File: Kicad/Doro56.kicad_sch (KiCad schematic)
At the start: 76 parts, among them J1 MJ-4PP-9, SW1 SW_Push_45deg, SW10 SW_Push_45deg, SW11 SW_Push_45deg, SW12 SW_Push_45deg, SW13 SW_Push_45deg, SW14 SW_Push_45deg, SW15 SW_Push_45deg, SW16 SW_Push_45deg, SW17 SW_Push_45deg, SW18 SW_Push_45deg, SW19 SW_Push_45deg, SW2 SW_Push_45deg, SW20 SW_Push_45deg, SW21 SW_Push_45deg, SW22 SW_Push_45deg, SW23 SW_Push_45deg, SW24 SW_Push_45deg, SW25 SW_Push_45deg, SW26 SW_Push_45deg, SW27 SW_Push_45deg, SW28 SW_Push_45deg, SW29 SW_Push_45deg, SW3 SW_Push_45deg, SW30 SW_Push_45deg, SW31 SW_Push_45deg, SW32 SW_Push_45deg, SW33 RotaryEncoder_Switch, SW34 SW_SPDT, SW4 SW_Push_45deg, SW5 SW_Push_45deg, SW6 SW_Push_45deg, SW7 SW_Push_45deg, SW8 SW_Push_45deg, SW9 SW_Push_45deg, U1 ProMicro

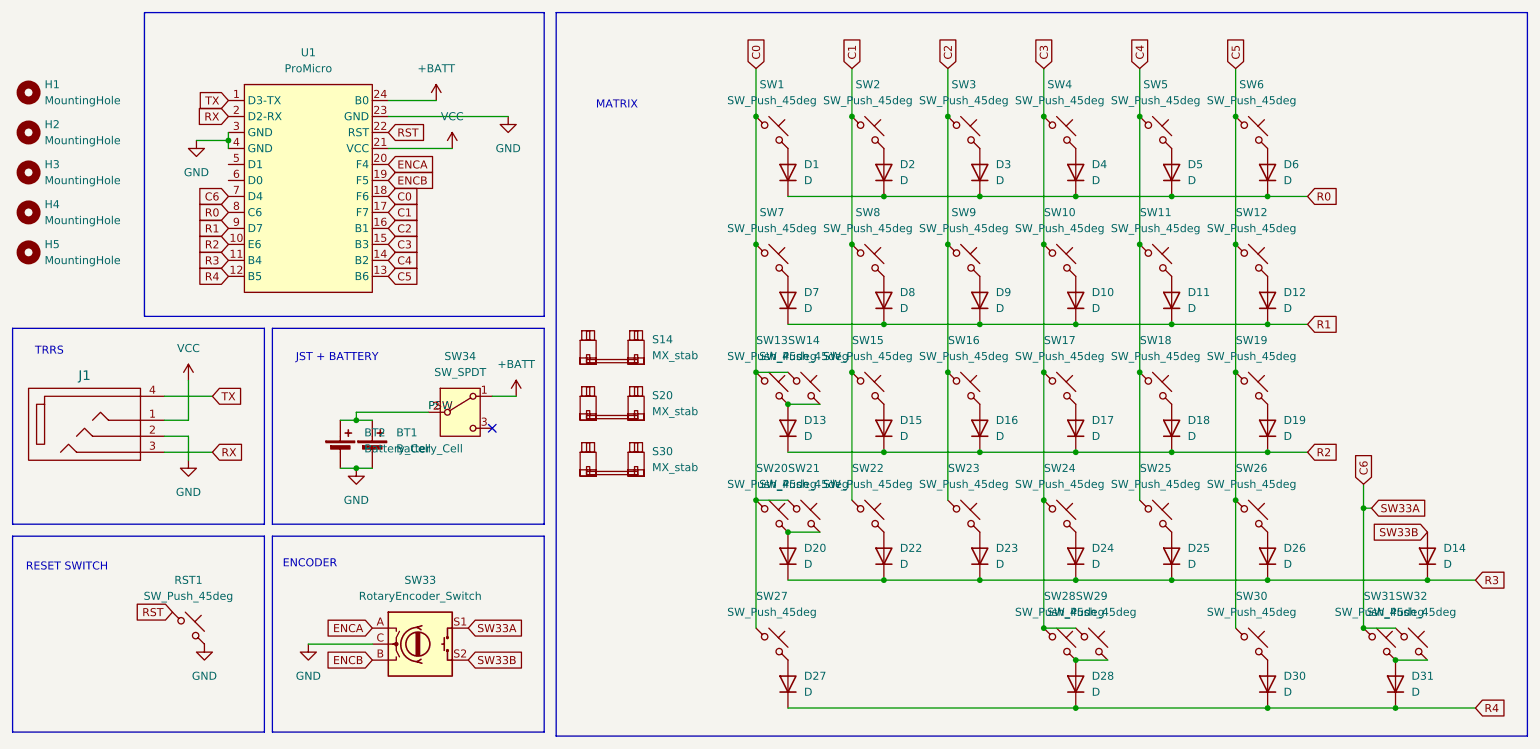
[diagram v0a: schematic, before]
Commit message: v1.1
v1.1 - Minor Edit
Caps and Enter Footprints: Changed to a reversible footprint (previously used two single key footprints rotated).
JST PH Footprint: Adjusted and relocated for increased flexibility.
PCB Cutout: Modified to remove blank space between Control and Alt keys, allowing space for a 402030 battery without increasing the case height clearance.
Plate: Slightly increased the cutout size for the rotary encoder.
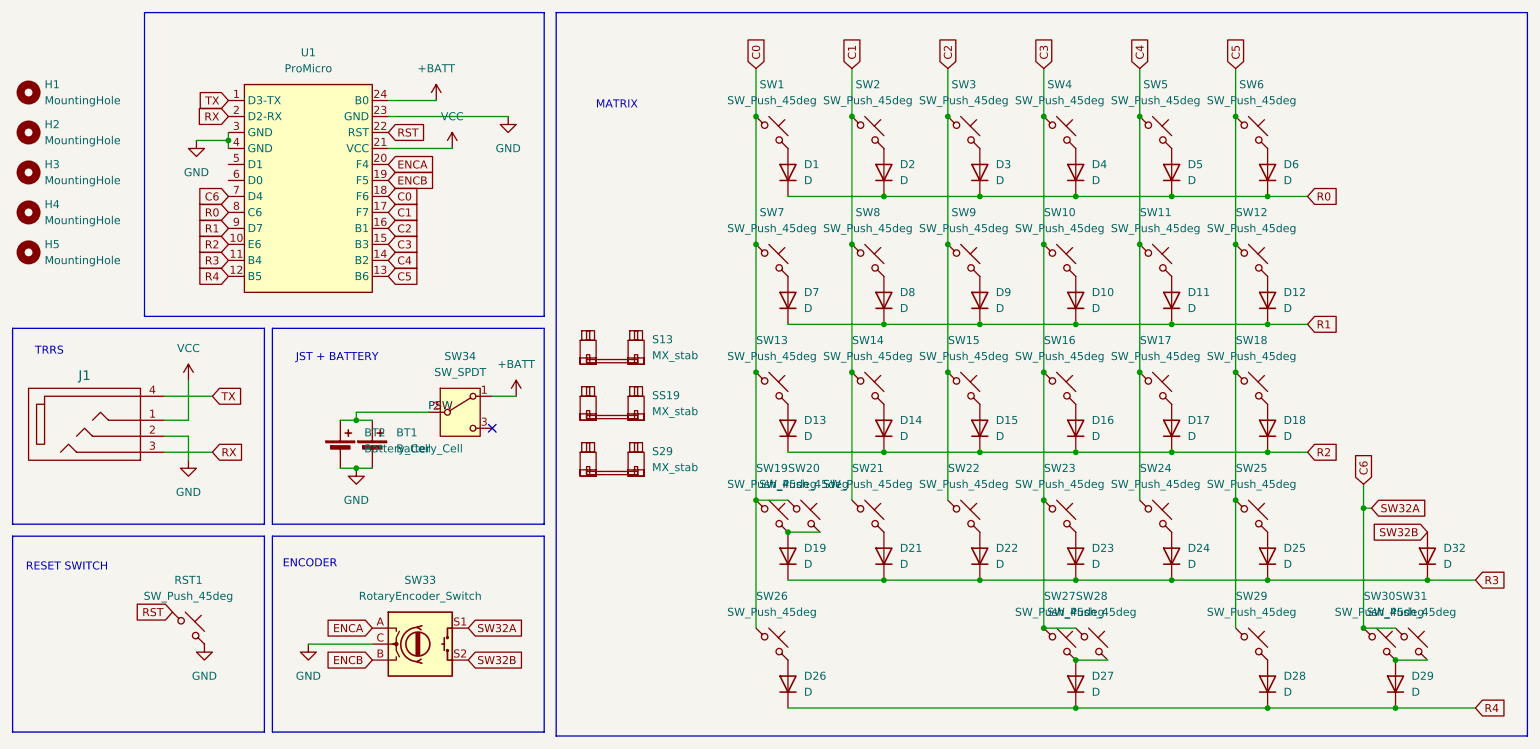
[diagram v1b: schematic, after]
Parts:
- removed SW14: SW_Push_45deg, GHN:MX 2.25U, symbol Switch:SW_Push_45deg
- BT1: footprint GHN:JST_PH_reversible -> GHN:JST_PH_reversible_vert
- SW13: footprint GHN:MX 1.75 STP 1.25 -> GHN:MX Rev 1U
- renumbered D15 to D14, D16 to D15, D17 to D16, D18 to D17, D19 to D18, D20 to D19, D22 to D21, D23 to D22, D24 to D23, D25 to D24, D26 to D25, D27 to D26, D28 to D27, D30 to D28, D31 to D29, D14 to D32, S14 to S13, S30 to S29, S20 to SS19, SW15 to SW14, SW16 to SW15, SW17 to SW16, SW18 to SW17, SW19 to SW18, SW20 to SW19, SW21 to SW20, SW22 to SW21, SW23 to SW22, SW24 to SW23, SW25 to SW24, SW26 to SW25, SW27 to SW26, SW28 to SW27, SW29 to SW28, SW30 to SW29, SW31 to SW30, SW32 to SW31
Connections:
- net SW33B renamed SW32B

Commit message: yeet lego case
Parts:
- renumbered SS19 to S19
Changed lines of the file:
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@@
 		(dnp no)
 		(fields_autoplaced yes)
-		(property "Reference" "SS19"
+		(property "Reference" "S19"
 			(at 142.24 77.3429 0)
 			(effects
@@
 			(project "Doro56"
 				(path "/66443d69-f594-44f0-97f8-81b5f08a0d21"
-					(reference "SS19")
+					(reference "S19")
 					(unit 1)
 				)

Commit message: 1.2
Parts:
- BT1: footprint GHN:JST_PH_reversible_vert -> GHN:JST_PH_2P_Reversible
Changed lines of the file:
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@@
 		(dnp no)
 		(property "Reference" "BT2"
-			(at 96.52 83.2484 0)
+			(at 88.9 83.312 0)
 			(effects
 				(font
@@
 		)
 		(property "Value" "Battery_Cell"
-			(at 96.52 85.7884 0)
+			(at 82.296 87.122 0)
 			(effects
 				(font
@@
 		(dnp no)
 		(property "Reference" "BT1"
-			(at 101.6 83.2484 0)
+			(at 99.822 83.312 0)
 			(effects
 				(font
@@
 		)
 		(property "Value" "Battery_Cell"
-			(at 101.6 85.7884 0)
+			(at 96.52 87.122 0)
 			(effects
 				(font
@@
 			)
 		)
-		(property "Footprint" "GHN:JST_PH_reversible_vert"
+		(property "Footprint" "GHN:JST_PH_2P_Reversible"
 			(at 97.79 84.836 90)
 			(effects
